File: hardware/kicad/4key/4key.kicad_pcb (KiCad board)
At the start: 2 copper layers, 87.2 x 70.6 mm, 39 parts, among them J1 USB_C_Receptacle, J2 SPARE / DEBUG, SW1 AGENT1, SW2 AGENT2, SW3 AGENT3, SW4 PTT, U1 ESP32-S3-WROOM-1-N16R8, U2 XL9555 / PCF8575 (TSSOP-24), U3 AP2112K-3.3, U4 74LVC1G17

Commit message: Fix real generator bugs found by an independent pre-fab hardware review
Verified all 41 ESP32-S3-WROOM-1 pins and all 24 XL9555 pins in
boarddef.py against their primary-source datasheets (not search-engine
summaries, which were caught being wrong twice: once claiming XL9555's
SDA/SCL were swapped, once claiming two WROOM-1 GND/thermal pins were
GPIOs). Both parts' full pin assignments match exactly.

An independent Opus review of the whole design caught three real issues
a pinout check alone couldn't:

- gen_pcb.py ignored a part's `nc` (no-connect) list entirely, while
  gen_sch.py respected it - real schematic/PCB drift for any pin that
  has both a plausible net name and an explicit no-connect (the last
  LED's DOUT, still called LEDCH%d with nothing next in the chain).
  Fixed by checking nc first in place_parts(), same as gen_sch.py.
- No bulk cap at U1's own +3V3 pin (nearest was ~37mm away). Added C9
  (10uF), T-tapped off the existing +3V3 B.Cu trunk - not literally at
  the pin, since the whole left margin is already packed solid; see the
  code comments for exactly where it landed and why.
- No USB ESD protection. Added D_ESD (USBLC6-2SC6 TVS array), pinout
  confirmed against the actual symbol KiCad ships, shunted across the
  existing USB_DP/USB_DM/+5V/GND nets. Left unrouted like the rest of
  the differential pair - this only adds the part to the schematic/BOM.

Also fixed a doc bug (gen_pcb.py's own comment on the mounting-hole
x-position didn't match the code) and a missing sym-lib-table entry for
the new ESD diode's symbol library.

All three tiers (4key/8key/12key) regenerated and re-verified: 0 DRC
violations, 0 ERC violations.

One real gap surfaced, not a code fix: boarddef.py's LED footprint
(plain SK6812MINI, not "-E") is internally consistent, but the
current-budget math elsewhere was computed against the wrong datasheet
("-E"'s) - needs the exact SKU locked down before ordering. Also
confirmed no enclosure/case file exists in this repo at a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
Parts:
- removed H36, H37: MountingHole_2.2mm_M2, MountingHole_2.2mm_M2
- added C9: 10u, C_0805_2012Metric_Pad1.18x1.45mm_HandSolder, F.Cu at (141.0, 133.0)
- added D_ESD: USBLC6-2SC6, SOT-23-6, F.Cu at (136.0, 124.0)
- added H40: MountingHole_2.2mm_M2, MountingHole_2.2mm_M2, F.Cu at (104.0, 166.6)
- added H41: MountingHole_2.2mm_M2, MountingHole_2.2mm_M2, F.Cu at (183.2, 166.6)
- moved H38 78.5 mm to (151.5, 104.0)
- moved H39 62.6 mm to (183.2, 104.0)
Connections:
- D4 pad 1: LEDCH4 -> (no net)
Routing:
- net +3V3: track 115.6 -> 123.1 mm, vias 2 -> 3

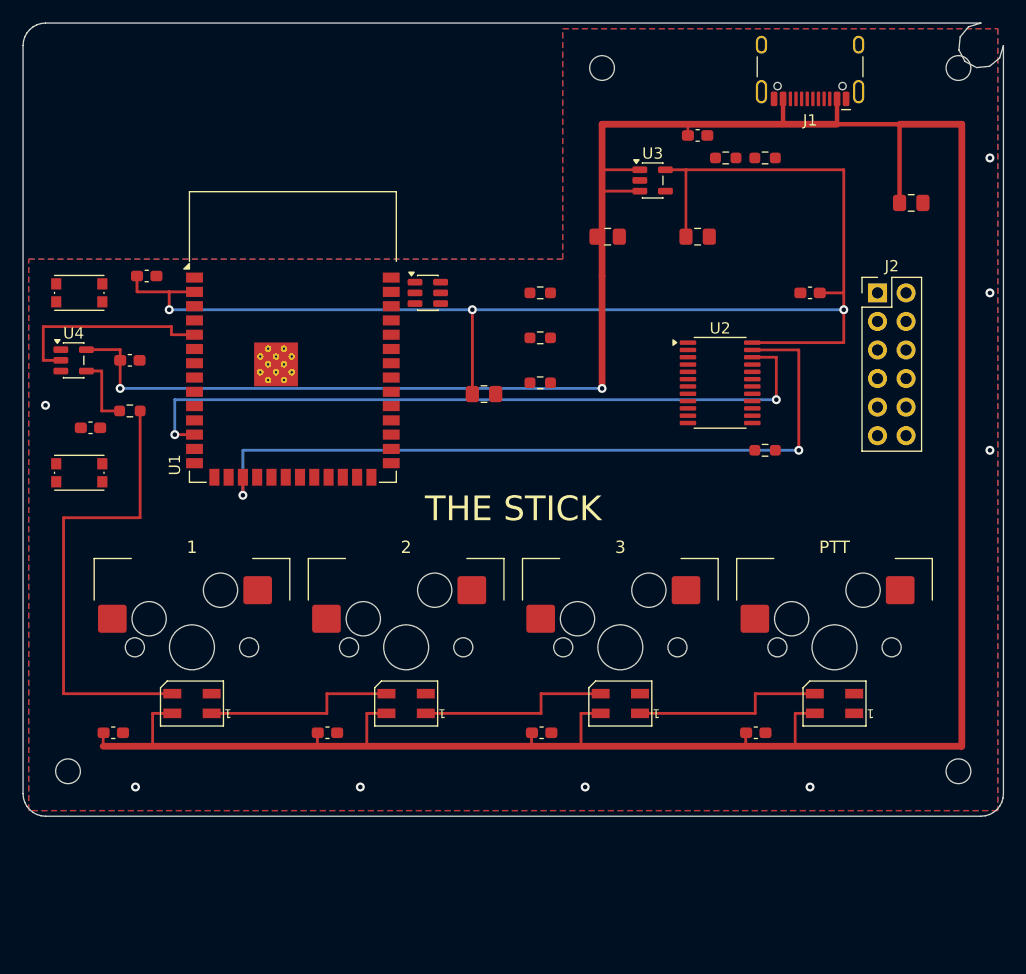
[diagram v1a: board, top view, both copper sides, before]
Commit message: Fix 4key I2C pull-up placement, grow the board, finish routing
Root-caused the 4key board's unrouted/short-prone corner: R4/R5 (the
I2C pull-ups for U2) were placed 16mm from the chip they serve, forcing
their traces across every other bus lane on the board. Moved them next
to U2 in boarddef.py, and grew STRIP 46mm -> 58mm (87.2x70.5mm ->
87.2x82.65mm) to give that whole corner real room — both the autorouter
and hand-routing had been failing to close the last nets in the old,
cramped layout.

route_strip()'s I2C section also hard-shorted SCL/SDA into +3V3 and
into each other once U2 moved down next to R4/R5 (caught by an
independent Opus review before fab) — rewritten to route both nets on
B.Cu the whole way, with small (0.5mm) vias where the standard 0.8mm
via can't fit the 0.65mm pin pitch.

Final DRC on the 4key board: 4 minor violations (2 pre-existing and
unrelated, 1 harmless dangling stub, cosmetic disconnected-but-same-net
ground-pour islands) and 2 low-priority unrouted pads in an extremely
congested corner (a spare header pin, a redundant pull-up supply leg) —
down from 39 unconnected items and multiple shorts earlier in this
pass. 8key/12key inherit the same STRIP/placement change and still
generate cleanly, but keep their own routing out of scope per the
existing "4key only" convention in gen_pcb.py.

Also adds hardware/enclosure/: a build123d-based parametric case
generator (hardware/enclosure/tools/gen_case.py) and its first-draft
4key tray/plate STLs, built from the real boarddef.py geometry rather
than guessed dimensions.

Boards ordered from JLCPCB at this routed revision.

Co-Authored-By: Claude Sonnet 5 <noreply@anthropic.com>
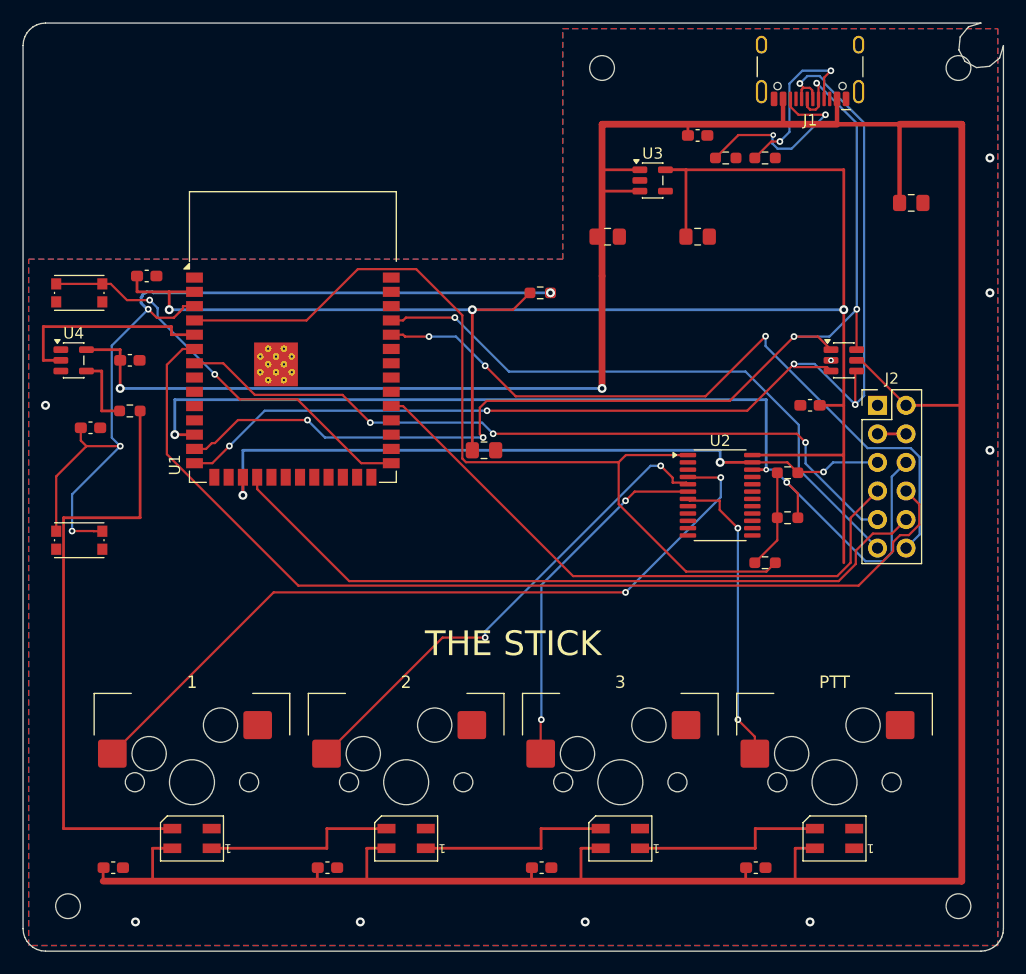
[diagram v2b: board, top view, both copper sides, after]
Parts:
- moved D_ESD 37.5 mm to (173.0, 130.0)
- moved R4 25.1 mm to (168.0, 140.0)
- moved R5 25.1 mm to (168.0, 144.0)
- moved D2 12.0 mm to (134.1, 172.5)
- moved SW2 12.0 mm to (134.1, 167.5)
- moved CL1 12.0 mm to (108.0, 175.1)
- moved CL2 12.0 mm to (127.1, 175.1)
- moved CL3 12.0 mm to (146.1, 175.1)
- moved CL4 12.0 mm to (165.2, 175.1)
- moved D1 12.0 mm to (115.0, 172.5)
- moved D3 12.0 mm to (153.1, 172.5)
- moved D4 12.0 mm to (172.2, 172.5)
- moved H40 12.0 mm to (104.0, 178.6)
- moved H41 12.0 mm to (183.2, 178.6)
- moved SW1 12.0 mm to (115.0, 167.5)
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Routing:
- net USB_DP: track 0.00 -> 107.1 mm, vias 0 -> 5
- net USB_DM: track 0.00 -> 100.4 mm, vias 0 -> 5
- net HDR_IO6: track 0.00 -> 89.0 mm
- net ~RESET: track 0.00 -> 82.5 mm, vias 0 -> 4
- net EXP_INT: track 0.00 -> 81.1 mm
- net KEY1: track 0.00 -> 68.3 mm, vias 0 -> 2
- net HDR_IO7: track 0.00 -> 67.6 mm, vias 0 -> 3
- net HDR_IO10: track 0.00 -> 65.1 mm
- net HDR_RXD0: track 0.00 -> 65.0 mm, vias 0 -> 3
- net HDR_IO38: track 0.00 -> 55.0 mm
- net HDR_TXD0: track 0.00 -> 54.2 mm, vias 0 -> 1
- net KEY2: track 0.00 -> 44.0 mm, vias 0 -> 2
- net +3V3: track 123.1 -> 164.1 mm
- net BOOT: track 0.00 -> 36.9 mm, vias 0 -> 2
- net KEY3: track 0.00 -> 31.5 mm, vias 0 -> 2
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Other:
- board size 87.2 x 70.6 mm -> 87.2 x 82.6 mm

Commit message: 4key r2: move hot-swap pads to B.Cu and fix r1's GND/3V3 opens
r1 put the Kailh socket pads on F.Cu, the side the switch plugs into, so
no key could connect. Socket pads now on B.Cu (footprint, generator and
4key board), with a via at each routed pad 1 to reach the F.Cu KEY trace.

DRC on r1's as-fabricated fills also showed the GND pour split into 8
islands (LDO, expander, CC pull-downs and ESD diode all cut off from USB
ground) and the I2C/INT pull-ups plus J2 pin 1 off +3V3. Added stitching
vias, routed the missing +3V3 links (J2 via FreeRouting), and cleared the
LEDCH0 / SW_RST and USB_DP / J1 clearance violations. 4key is now DRC
clean with 0 unconnected items.

Co-Authored-By: Claude Opus 5.5 <noreply@anthropic.com>
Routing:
- net +3V3: track 164.1 -> 165.5 mm, vias 3 -> 5
- net GND: track 2.54 -> 3.88 mm, vias 9 -> 18
- net KEY4: vias 2 -> 3
- net KEY3: vias 2 -> 3
- net KEY2: vias 2 -> 3
- net KEY1: vias 2 -> 3
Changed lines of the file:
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@@
 			(at -7.085 -2.54)
 			(size 2.55 2.5)
-			(layers "F.Cu" "F.Mask" "F.Paste")
+			(layers "B.Cu" "B.Mask" "B.Paste")
 			(roundrect_rratio 0.1)
 			(net "KEY2")
@@
 			(at 5.842 -5.08)
 			(size 2.55 2.5)
-			(layers "F.Cu" "F.Mask" "F.Paste")
+			(layers "B.Cu" "B.Mask" "B.Paste")
 			(roundrect_rratio 0.1)
 			(net "GND")
@@
 			(at -7.085 -2.54)
 			(size 2.55 2.5)
-			(layers "F.Cu" "F.Mask" "F.Paste")
+			(layers "B.Cu" "B.Mask" "B.Paste")
 			(roundrect_rratio 0.1)
 			(net "KEY1")
@@
 			(at 5.842 -5.08)
 			(size 2.55 2.5)
-			(layers "F.Cu" "F.Mask" "F.Paste")
+			(layers "B.Cu" "B.Mask" "B.Paste")
 			(roundrect_rratio 0.1)
 			(net "GND")
@@
 			(at -7.085 -2.54)
 			(size 2.55 2.5)
-			(layers "F.Cu" "F.Mask" "F.Paste")
+			(layers "B.Cu" "B.Mask" "B.Paste")
 			(roundrect_rratio 0.1)
 			(net "KEY3")
@@
 			(at 5.842 -5.08)
 			(size 2.55 2.5)
-			(layers "F.Cu" "F.Mask" "F.Paste")
+			(layers "B.Cu" "B.Mask" "B.Paste")
 			(roundrect_rratio 0.1)
 			(net "GND")
@@
 			(at -7.085 -2.54)
 			(size 2.55 2.5)
-			(layers "F.Cu" "F.Mask" "F.Paste")
+			(layers "B.Cu" "B.Mask" "B.Paste")
 			(roundrect_rratio 0.1)
 			(net "KEY4")
@@
 			(at 5.842 -5.08)
 			(size 2.55 2.5)
-			(layers "F.Cu" "F.Mask" "F.Paste")
+			(layers "B.Cu" "B.Mask" "B.Paste")
 			(roundrect_rratio 0.1)
 			(net "GND")
@@
 		(net "GND")
 	)
+	(segment
+		(start 163.412 112)
+		(end 163.9 110.75)
+		(width 0.25)
+		(layer "F.Cu")
+		(net "GND")
+	)
+	(via
+		(at 150.18 129.88)
+		(size 0.8)
+		(drill 0.4)
+		(layers "F.Cu" "B.Cu")
+		(net "GND")
+	)
+	(via
+		(at 112.99 128.88)
+		(size 0.8)
+		(drill 0.4)
+		(layers "F.Cu" "B.Cu")
+		(net "GND")
+	)
 	(via
 		(at 150 179.95)
@@
 	)
 	(via
+		(at 163.9 110.75)
+		(size 0.8)
+		(drill 0.4)
+		(layers "F.Cu" "B.Cu")
+		(net "GND")
+	)
+	(via
+		(at 160.79 139.13)
+		(size 0.8)
+		(drill 0.4)
+		(layers "F.Cu" "B.Cu")
+		(net "GND")
+	)
+	(via
 		(at 186 112)
 		(size 0.8)
@@
 	)
 	(via
+		(at 162.3 121.3)
+		(size 0.8)
+		(drill 0.4)
+		(layers "F.Cu" "B.Cu")
+		(net "GND")
+	)
+	(via
+		(at 130.199999 122.99)
+		(size 0.8)
+		(drill 0.4)
+		(layers "F.Cu" "B.Cu")
+		(net "GND")
+	)
+	(via
 		(at 102 134)
 		(size 0.8)
@@
 	)
 	(via
+		(at 161.04 144.7)
+		(size 0.8)
+		(drill 0.4)
+		(layers "F.Cu" "B.Cu")
+		(net "GND")
+	)
+	(via
+		(at 175.72 121.45)
+		(size 0.8)
+		(drill 0.4)
+		(layers "F.Cu" "B.Cu")
+		(net "GND")
+	)
+	(via
+		(at 156.73 135.45)
+		(size 0.8)
+		(drill 0.4)
+		(layers "F.Cu" "B.Cu")
+		(net "GND")
+	)
+	(via
 		(at 186 124)
 		(size 0.8)
@@
 	)
 	(segment
+		(start 167.088 138.425)
+		(end 164.862 138.425)
+		(width 0.25)
+		(layer "F.Cu")
+		(net "+3V3")
+	)
+	(segment
+		(start 173 134)
+		(end 173 138.425)
+		(width 0.25)
+		(layer "F.Cu")
+		(net "+3V3")
+	)
+	(segment
+		(start 173.581 134.581)
+		(end 174.268 134.581)
+		(width 0.25)
+		(layer "F.Cu")
+		(net "+3V3")
+	)
+	(segment
 		(start 110.1375 122.5)
 		(end 110.138 122.5)
@@
 	)
 	(segment
+		(start 174.848 134)
+		(end 176 134)
+		(width 0.25)
+		(layer "F.Cu")
+		(net "+3V3")
+	)
+	(segment
+		(start 174.268 134.581)
+		(end 174.848 134)
+		(width 0.25)
+		(layer "F.Cu")
+		(net "+3V3")
+	)
+	(segment
 		(start 113 123.91)
 		(end 110.138 123.91)
@@
 	)
 	(segment
+		(start 164.862 138.425)
+		(end 165.3 137.4)
+		(width 0.25)
+		(layer "F.Cu")
+		(net "+3V3")
+	)
+	(segment
 		(start 157.138 113.05)
 		(end 157.1375 113.05)
@@
 	)
 	(segment
+		(start 173 134)
+		(end 173.581 134.581)
+		(width 0.25)
+		(layer "F.Cu")
+		(net "+3V3")
+	)
+	(segment
 		(start 167.0875 146)
 		(end 165.0875 148)
@@
 	(segment
 		(start 173 113.05)
-		(end 173 148)
+		(end 173 125.5)
 		(width 0.25)
 		(layer "F.Cu")
@@
 	(segment
 		(start 173 138.425)
-		(end 164.862 138.425)
+		(end 167.088 138.425)
 		(width 0.25)
 		(layer "F.Cu")
@@
 		(net "+3V3")
 	)
+	(segment
+		(start 173 125.5)
+		(end 173 134)
+		(width 0.25)
+		(layer "F.Cu")
+		(net "+3V3")
+	)
 	(via
 		(at 113 125.5)
@@
 	)
 	(via
+		(at 167.088 142)
+		(size 0.8)
+		(drill 0.4)
+		(layers "F.Cu" "B.Cu")
+		(net "+3V3")
+	)
+	(via
 		(at 139.962 125.5)
 		(size 0.8)
@@
 	)
 	(via
+		(at 165.3 137.4)
+		(size 0.8)
+		(drill 0.4)
+		(layers "F.Cu" "B.Cu")
+		(net "+3V3")
+	)
+	(via
 		(at 173 125.5)
 		(size 0.8)
@@
 	)
 	(segment
+		(start 165.3 137.4)
+		(end 165.3 142)
+		(width 0.25)
+		(layer "B.Cu")
+		(net "+3V3")
+	)
+	(segment
 		(start 173 125.5)
 		(end 113 125.5)
@@
 	)
 	(segment
+		(start 165.3 142)
+		(end 167.088 142)
+		(width 0.25)
+		(layer "B.Cu")
+		(net "+3V3")
+	)
+	(segment
 		(start 115.25 125.18)
 		(end 114.2233 125.18)
@@
 	)
 	(segment
-		(start 104.3597 145.1832)
-		(end 106.2815 145.1832)
+		(start 104.6 145.183)
+		(end 106.281 145.183)
 		(width 0.2)
 		(layer "F.Cu")
@@
 	)
 	(via
-		(at 104.3597 145.1832)
+		(at 104.6 145.183)
 		(size 0.6)
 		(drill 0.3)
@@
 	)
 	(segment
-		(start 104.3597 145.1832)
-		(end 104.3597 141.9236)
+		(start 104.6 145.183)
+		(end 104.6 141.924)
 		(width 0.2)
 		(layer "B.Cu")
@@
 	)
 	(segment
-		(start 104.3597 141.9236)
-		(end 108.6503 137.633)
+		(start 104.6 141.924)
+		(end 108.65 137.633)
 		(width 0.2)
 		(layer "B.Cu")
@@
 	)
 	(via
+		(at 126.99 164.985)
+		(size 0.8)
+		(drill 0.4)
+		(layers "F.Cu" "B.Cu")
+		(net "KEY2")
+	)
+	(via
 		(at 141.1038 154.6601)
 		(size 0.6)
@@
 	)
 	(segment
-		(start 170.1923 105.9753)
-		(end 169.9789 105.7619)
+		(start 170.062 105.762)
+		(end 169.979 105.762)
 		(width 0.2)
 		(layer "F.Cu")
@@
 	)
 	(segment
-		(start 170.25 106.3472)
-		(end 170.1923 106.2895)
+		(start 170.25 106.347)
+		(end 170.25 105.95)
 		(width 0.2)
 		(layer "F.Cu")
@@
 	)
 	(segment
-		(start 170.1923 106.2895)
-		(end 170.1923 105.9753)
+		(start 170.25 105.95)
+		(end 170.062 105.762)
 		(width 0.2)
 		(layer "F.Cu")
@@
 	)
 	(via
+		(at 107.94 164.985)
+		(size 0.8)
+		(drill 0.4)
+		(layers "F.Cu" "B.Cu")
+		(net "KEY1")
+	)
+	(via
 		(at 153.5898 150.6405)
 		(size 0.6)
@@
 	)
 	(via
+		(at 146.04 164.985)
+		(size 0.8)
+		(drill 0.4)
+		(layers "F.Cu" "B.Cu")
+		(net "KEY3")
+	)
+	(via
 		(at 146.0982 161.9618)
 		(size 0.6)
@@
 	)
 	(via
+		(at 165.09 164.985)
+		(size 0.8)
+		(drill 0.4)
+		(layers "F.Cu" "B.Cu")
+		(net "KEY4")
+	)
+	(via
 		(at 163.5786 161.9618)
 		(size 0.6)
@@
 	)
 	(segment
-		(start 103.6 144)
-		(end 103.6 171.65)
+		(start 103.8 144)
+		(end 103.8 171.65)
 		(width 0.25)
 		(layer "F.Cu")
@@
 	)
 	(segment
-		(start 103.6 171.65)
+		(start 103.8 171.65)
 		(end 113.275 171.65)
 		(width 0.25)
@@
 	(segment
 		(start 110.412 144)
-		(end 103.6 144)
+		(end 103.8 144)
 		(width 0.25)
 		(layer "F.Cu")
